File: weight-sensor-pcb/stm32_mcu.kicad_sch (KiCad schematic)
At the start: 1 part, among them U3 STM32G431KBTx

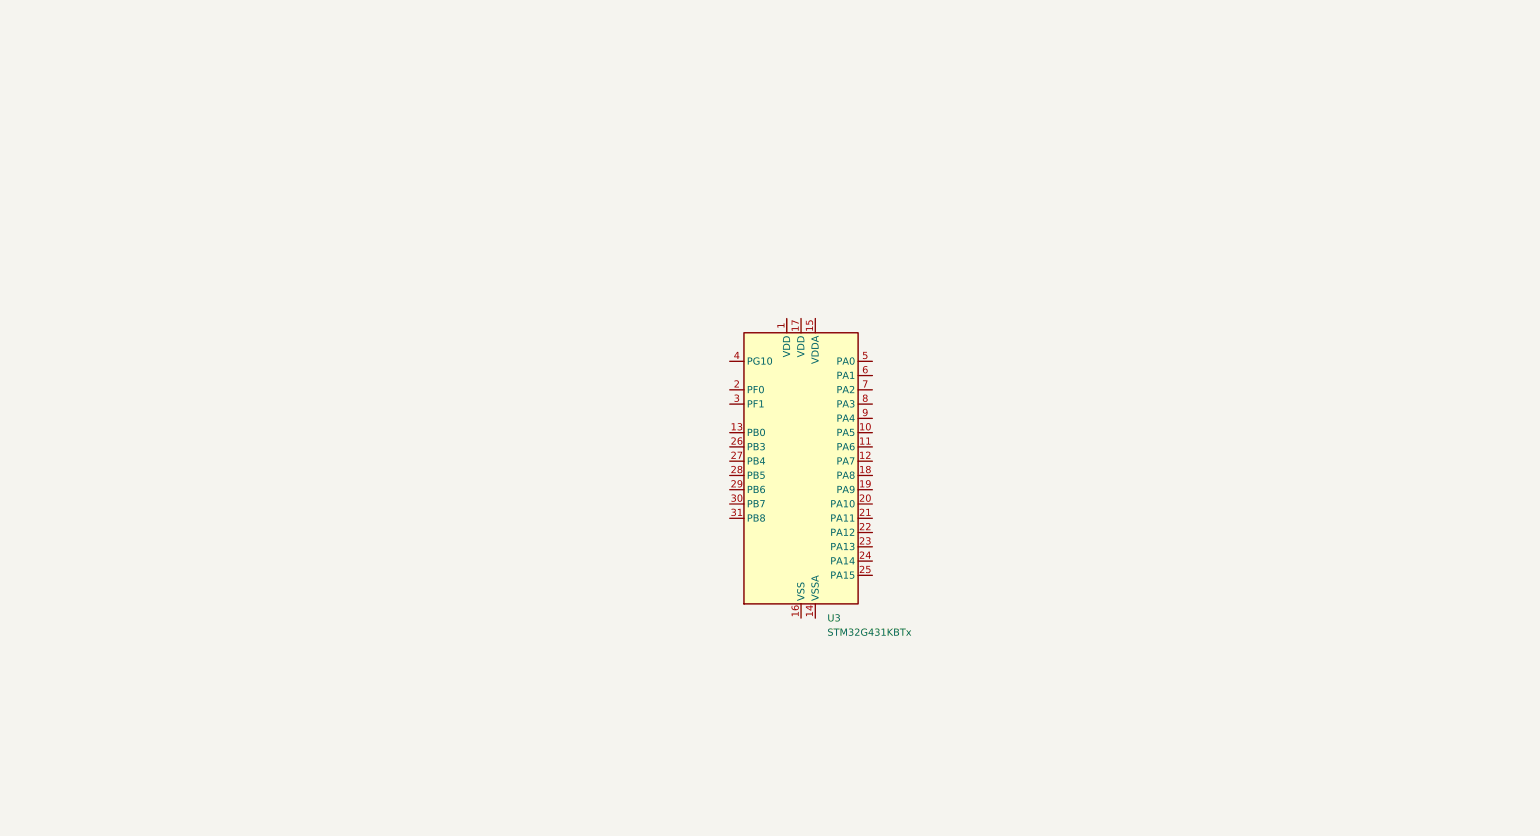
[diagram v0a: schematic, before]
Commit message: Swap MCU, add Library Loader integration
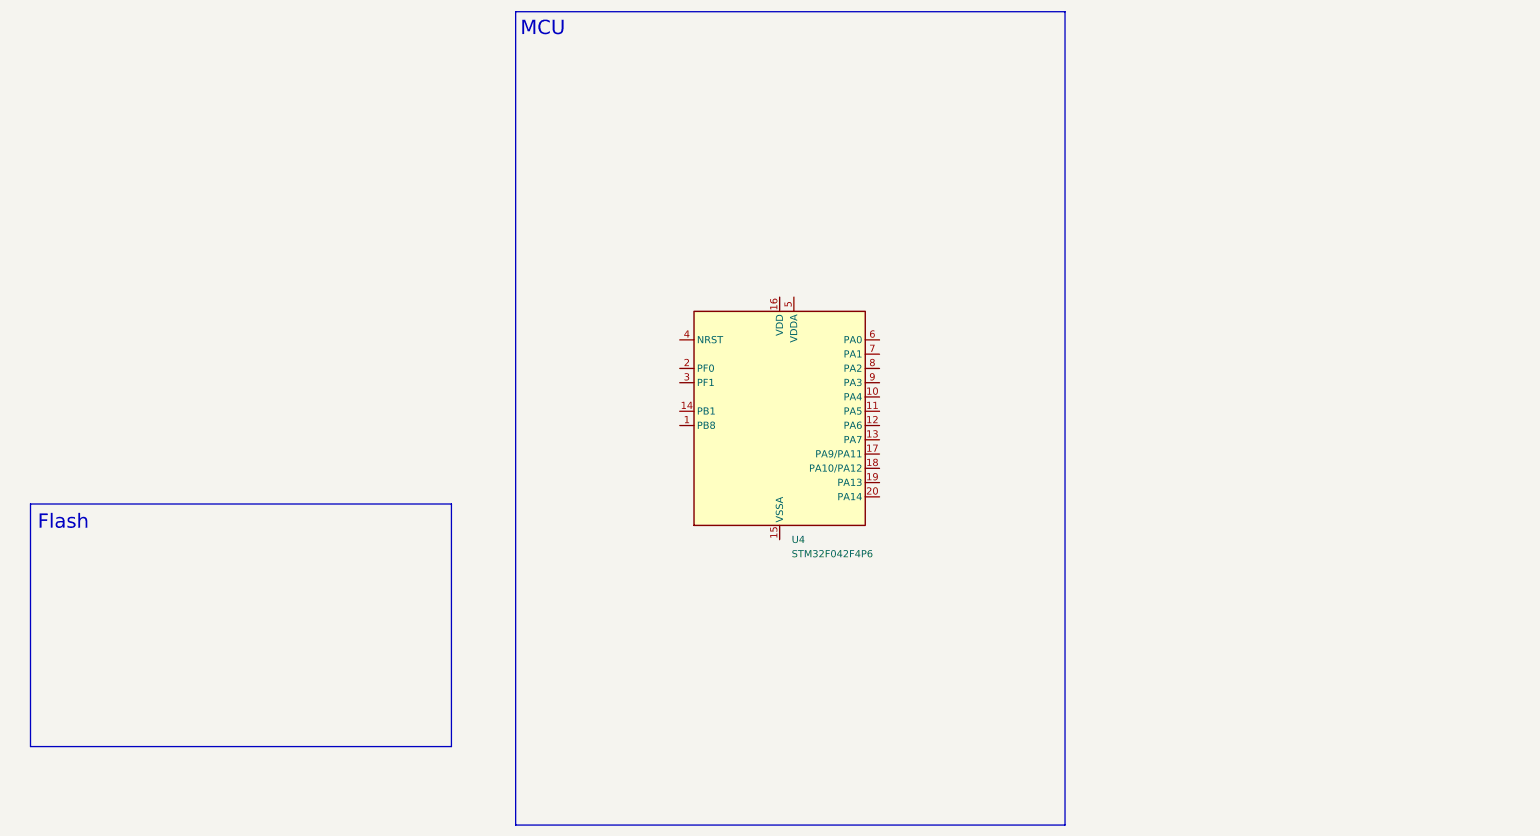
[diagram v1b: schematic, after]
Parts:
- removed U3: STM32G431KBTx, Package_QFP:LQFP-32_7x7mm_P0.8mm, symbol MCU_ST_STM32G4:STM32G431KBTx
- added U4: STM32F042F4P6, Package_SO:TSSOP-20_4.4x6.5mm_P0.65mm, symbol MCU_ST_STM32F0:STM32F042F4Px
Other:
- note added: "Flash"
- note added: "MCU"
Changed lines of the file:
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@@
 		(title "STM32 Microcontroller")
 	)
+	(rectangle
+		(start 15.24 101.6)
+		(end 90.17 144.78)
+		(stroke
+			(width 0)
+			(type default)
+		)
+		(fill
+			(type none)
+		)
+	)
+	(rectangle
+		(start 101.6 13.97)
+		(end 199.39 158.75)
+		(stroke
+			(width 0)
+			(type default)
+		)
+		(fill
+			(type none)
+		)
+	)
+	(text "Flash"
+		(exclude_from_sim no)
+		(at 21.082 104.902 0)
+		(effects
+			(font
+				(size 2.54 2.54)
+			)
+		)
+	)
+	(text "MCU"
+		(exclude_from_sim no)
+		(at 106.426 17.018 0)
+		(effects
+			(font
+				(size 2.54 2.54)
+			)
+		)
+	)
 	(symbol
-		(lib_id "MCU_ST_STM32G4:STM32G431KBTx")
-		(at 152.4 96.52 0)
+		(lib_id "MCU_ST_STM32F0:STM32F042F4Px")
+		(at 148.59 87.63 0)
 		(unit 1)
 		(exclude_from_sim no)
@@
 		(dnp no)
 		(fields_autoplaced yes)
-		(property "Reference" "U3"
-			(at 157.0833 121.92 0)
+		(property "Reference" "U4"
+			(at 150.7333 107.95 0)
 			(effects
 				(font
@@
 			)
 		)
-		(property "Value" "STM32G431KBTx"
-			(at 157.0833 124.46 0)
+		(property "Value" "STM32F042F4P6"
+			(at 150.7333 110.49 0)
 			(effects
 				(font
@@
 			)
 		)
-		(property "Footprint" "Package_QFP:LQFP-32_7x7mm_P0.8mm"
-			(at 142.24 119.38 0)
+		(property "Footprint" "Package_SO:TSSOP-20_4.4x6.5mm_P0.65mm"
+			(at 133.35 105.41 0)
 			(effects
 				(font
@@
 			)
 		)
-		(property "Datasheet" "https://www.st.com/resource/en/datasheet/stm32g431kb.pdf"
-			(at 152.4 96.52 0)
+		(property "Datasheet" "https://www.st.com/resource/en/datasheet/stm32f042f4.pdf"
+			(at 148.59 87.63 0)
 			(effects
 				(font
@@
 			)
 		)
-		(property "Description" "STMicroelectronics Arm Cortex-M4 MCU, 128KB flash, 32KB RAM, 170 MHz, 1.71-3.6V, 26 GPIO, LQFP32"
-			(at 152.4 96.52 0)
+		(property "Description" "STMicroelectronics Arm Cortex-M0 MCU, 16KB flash, 6KB RAM, 48 MHz, 2.0-3.6V, 16 GPIO, TSSOP20"
+			(at 148.59 87.63 0)
 			(effects
 				(font
@@
 			)
 		)
+		(pin "8"
+		)
+		(pin "7"
+		)
+		(pin "6"
+		)
+		(pin "17"
+		)
+		(pin "3"
+		)
+		(pin "10"
+		)
+		(pin "12"
+		)
+		(pin "13"
+		)
+		(pin "4"
+		)
+		(pin "1"
+		)
+		(pin "11"
+		)
 		(pin "18"
 		)
-		(pin "21"
+		(pin "16"
+		)
+		(pin "2"
+		)
+		(pin "9"
+		)
+		(pin "5"
+		)
+		(pin "14"
+		)
+		(pin "15"
 		)
 		(pin "20"
@@
 		(pin "19"
 		)
-		(pin "22"
-		)
-		(pin "23"
-		)
-		(pin "24"
-		)
-		(pin "25"
-		)
-		(pin "4"
-		)
-		(pin "2"
-		)
-		(pin "3"
-		)
-		(pin "13"
-		)
-		(pin "26"
-		)
-		(pin "27"
-		)
-		(pin "28"
-		)
-		(pin "29"
-		)
-		(pin "30"
-		)
-		(pin "31"
-		)
-		(pin "1"
-		)
-		(pin "17"
-		)
-		(pin "16"
-		)
-		(pin "32"
-		)
-		(pin "15"
-		)
-		(pin "14"
-		)
-		(pin "5"
-		)
-		(pin "6"
-		)
-		(pin "7"
-		)
-		(pin "8"
-		)
-		(pin "9"
-		)
-		(pin "10"
-		)
-		(pin "11"
-		)
-		(pin "12"
-		)
 		(instances
 			(project ""
 				(path "/030ca1f5-68f0-4323-9a91-656d7965b13e/d023421c-1516-46ef-aa61-fab015035186"
-					(reference "U3")
+					(reference "U4")
 					(unit 1)
 				)

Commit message: Add Serial Connection and CAN Transceiver
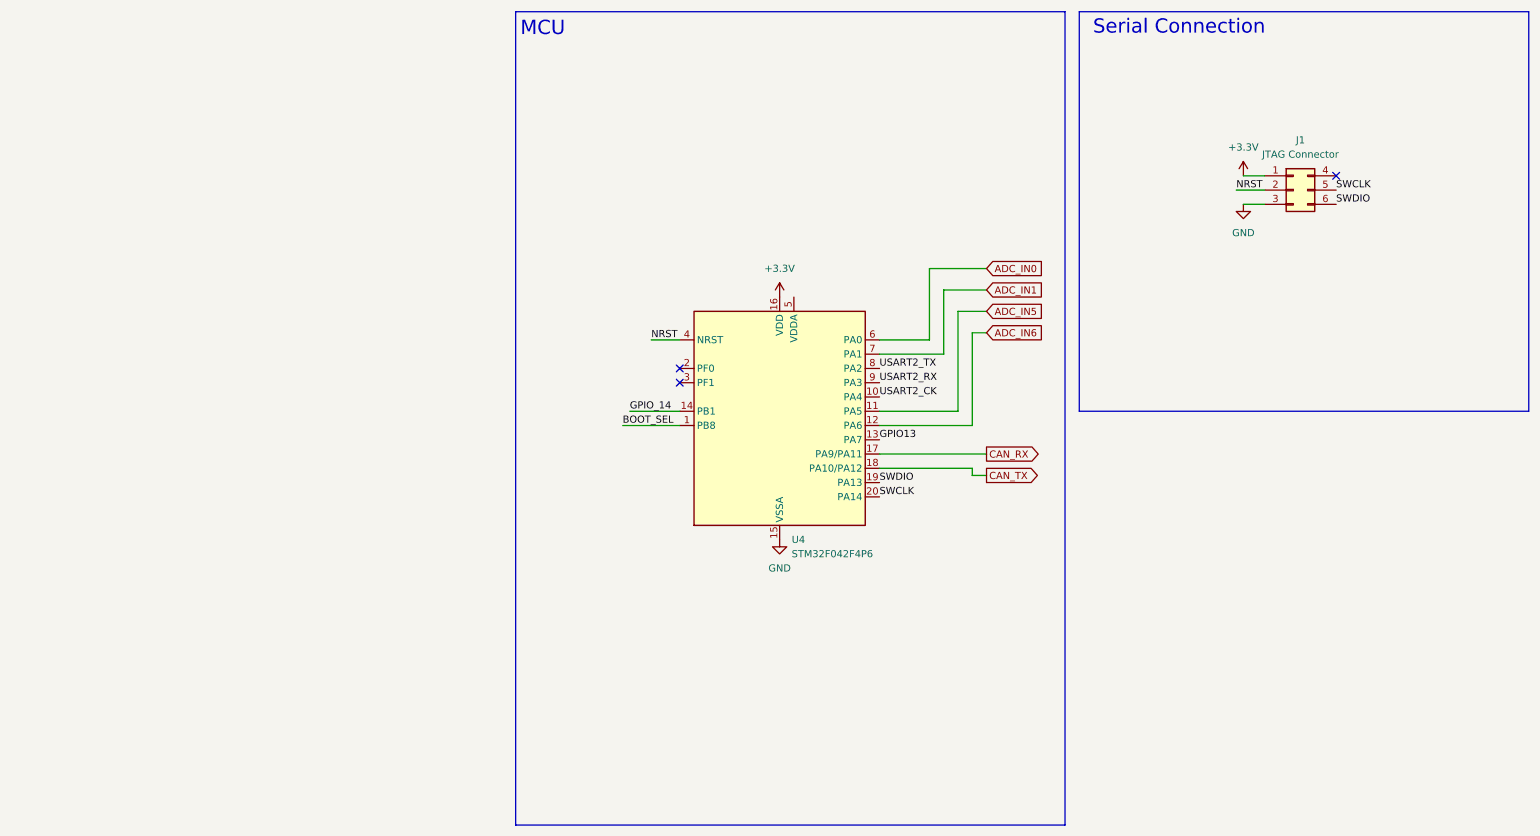
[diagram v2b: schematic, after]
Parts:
- added J1: JTAG Connector, Capstone:TC2030-IDC-NL, symbol Connector_Generic:Conn_02x03_Top_Bottom
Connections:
- net BOOT_SEL: now reaches U4.1 (PB8)
- net USART2_CK: now reaches U4.10 (PA4)
- net ADC_IN5: now reaches U4.11 (PA5)
- net ADC_IN6: now reaches U4.12 (PA6)
- net GPIO13: now reaches U4.13 (PA7)
- net GPIO_14: now reaches U4.14 (PB1)
- net GND: now reaches U4.15 (VSSA)
- net GND: now also J1.3 (Pin_3)
- net +3.3V: now reaches U4.16 (VDD)
- net +3.3V: now also J1.1 (Pin_1)
- net CAN_RX: now reaches U4.17 (PA9/PA11)
- net CAN_TX: now reaches U4.18 (PA10/PA12)
- net SWDIO: now reaches U4.19 (PA13)
- net SWDIO: now also J1.6 (Pin_6)
- net SWCLK: now reaches U4.20 (PA14)
- net SWCLK: now also J1.5 (Pin_5)
- net NRST: now reaches U4.4 (NRST)
- net NRST: now also J1.2 (Pin_2)
- net ADC_IN0: now reaches U4.6 (PA0)
- net ADC_IN1: now reaches U4.7 (PA1)
- net USART2_TX: now reaches U4.8 (PA2)
- net USART2_RX: now reaches U4.9 (PA3)
- no-connect marks 0 -> 3
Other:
- note added: "Serial Connection"
- note removed: "Flash"

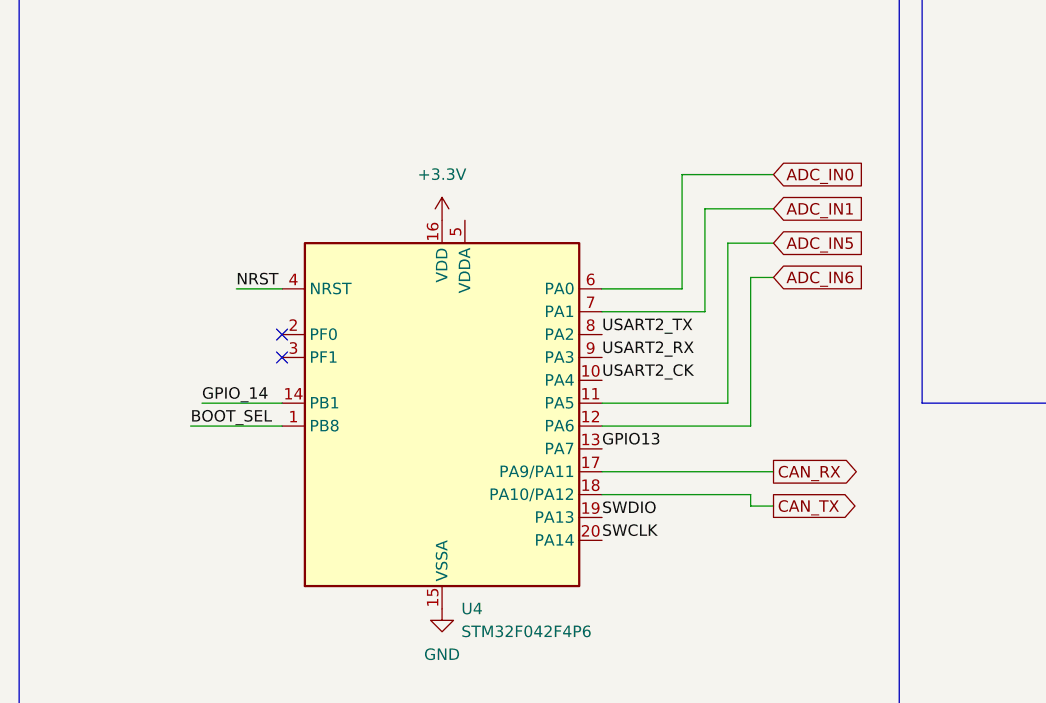
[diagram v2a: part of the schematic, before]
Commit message: Add hierarchial labels to MCU and CAN Interface sheets
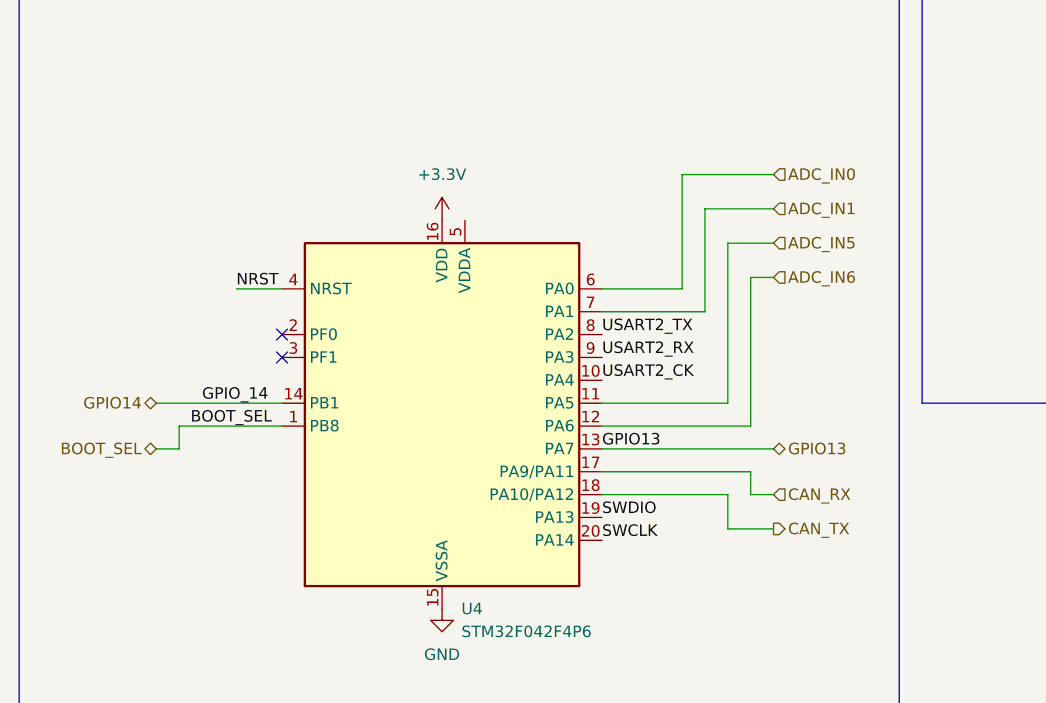
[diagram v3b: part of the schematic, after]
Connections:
- net GPIO_14 renamed GPIO14
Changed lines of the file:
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@@
 	(wire
 		(pts
-			(xy 120.65 87.63) (xy 130.81 87.63)
+			(xy 116.84 90.17) (xy 119.38 90.17)
 		)
 		(stroke
@@
 	(wire
 		(pts
+			(xy 182.88 92.71) (xy 166.37 92.71)
+		)
+		(stroke
+			(width 0)
+			(type default)
+		)
+	)
+	(wire
+		(pts
 			(xy 182.88 71.12) (xy 182.88 87.63)
 		)
@@
 	(wire
 		(pts
+			(xy 119.38 87.63) (xy 130.81 87.63)
+		)
+		(stroke
+			(width 0)
+			(type default)
+		)
+	)
+	(wire
+		(pts
 			(xy 175.26 59.69) (xy 175.26 72.39)
 		)
@@
 	(wire
 		(pts
-			(xy 121.92 85.09) (xy 130.81 85.09)
+			(xy 119.38 90.17) (xy 119.38 87.63)
+		)
+		(stroke
+			(width 0)
+			(type default)
+		)
+	)
+	(wire
+		(pts
+			(xy 185.42 90.17) (xy 166.37 90.17)
+		)
+		(stroke
+			(width 0)
+			(type default)
+		)
+	)
+	(wire
+		(pts
+			(xy 116.84 85.09) (xy 130.81 85.09)
 		)
 		(stroke
@@
 	(wire
 		(pts
-			(xy 185.42 96.52) (xy 182.88 96.52)
-		)
-		(stroke
-			(width 0)
-			(type default)
-		)
-	)
-	(wire
-		(pts
-			(xy 185.42 92.71) (xy 166.37 92.71)
+			(xy 185.42 99.06) (xy 180.34 99.06)
+		)
+		(stroke
+			(width 0)
+			(type default)
+		)
+	)
+	(wire
+		(pts
+			(xy 185.42 95.25) (xy 182.88 95.25)
 		)
 		(stroke
@@
 	(wire
 		(pts
-			(xy 182.88 95.25) (xy 166.37 95.25)
+			(xy 182.88 95.25) (xy 182.88 92.71)
+		)
+		(stroke
+			(width 0)
+			(type default)
+		)
+	)
+	(wire
+		(pts
+			(xy 180.34 95.25) (xy 166.37 95.25)
 		)
 		(stroke
@@
 	(wire
 		(pts
-			(xy 182.88 96.52) (xy 182.88 95.25)
+			(xy 180.34 99.06) (xy 180.34 95.25)
 		)
 		(stroke
@@
 		)
 	)
-	(global_label "CAN_TX"
+	(hierarchical_label "CAN_TX"
 		(shape output)
-		(at 185.42 96.52 0)
-		(fields_autoplaced yes)
-		(effects
-			(font
-				(size 1.27 1.27)
-			)
-			(justify left)
-		)
-		(property "Intersheetrefs" "${INTERSHEET_REFS}"
-			(at 195.239 96.52 0)
-			(effects
-				(font
-					(size 1.27 1.27)
-				)
-				(justify left)
-				(hide yes)
-			)
-		)
-	)
-	(global_label "ADC_IN5"
+		(at 185.42 99.06 0)
+		(effects
+			(font
+				(size 1.27 1.27)
+			)
+			(justify left)
+		)
+	)
+	(hierarchical_label "ADC_IN6"
+		(shape input)
+		(at 185.42 71.12 0)
+		(effects
+			(font
+				(size 1.27 1.27)
+			)
+			(justify left)
+		)
+	)
+	(hierarchical_label "GPIO13"
+		(shape bidirectional)
+		(at 185.42 90.17 0)
+		(effects
+			(font
+				(size 1.27 1.27)
+			)
+			(justify left)
+		)
+	)
+	(hierarchical_label "GPIO14"
+		(shape bidirectional)
+		(at 116.84 85.09 180)
+		(effects
+			(font
+				(size 1.27 1.27)
+			)
+			(justify right)
+		)
+	)
+	(hierarchical_label "ADC_IN5"
 		(shape input)
 		(at 185.42 67.31 0)
-		(fields_autoplaced yes)
-		(effects
-			(font
-				(size 1.27 1.27)
-			)
-			(justify left)
-		)
-		(property "Intersheetrefs" "${INTERSHEET_REFS}"
-			(at 196.1462 67.31 0)
-			(effects
-				(font
-					(size 1.27 1.27)
-				)
-				(justify left)
-				(hide yes)
-			)
-		)
-	)
-	(global_label "CAN_RX"
-		(shape output)
-		(at 185.42 92.71 0)
-		(fields_autoplaced yes)
-		(effects
-			(font
-				(size 1.27 1.27)
-			)
-			(justify left)
-		)
-		(property "Intersheetrefs" "${INTERSHEET_REFS}"
-			(at 195.5414 92.71 0)
-			(effects
-				(font
-					(size 1.27 1.27)
-				)
-				(justify left)
-				(hide yes)
-			)
-		)
-	)
-	(global_label "ADC_IN0"
+		(effects
+			(font
+				(size 1.27 1.27)
+			)
+			(justify left)
+		)
+	)
+	(hierarchical_label "CAN_RX"
+		(shape input)
+		(at 185.42 95.25 0)
+		(effects
+			(font
+				(size 1.27 1.27)
+			)
+			(justify left)
+		)
+	)
+	(hierarchical_label "ADC_IN0"
 		(shape input)
 		(at 185.42 59.69 0)
-		(fields_autoplaced yes)
-		(effects
-			(font
-				(size 1.27 1.27)
-			)
-			(justify left)
-		)
-		(property "Intersheetrefs" "${INTERSHEET_REFS}"
-			(at 196.1462 59.69 0)
-			(effects
-				(font
-					(size 1.27 1.27)
-				)
-				(justify left)
-				(hide yes)
-			)
-		)
-	)
-	(global_label "ADC_IN1"
+		(effects
+			(font
+				(size 1.27 1.27)
+			)
+			(justify left)
+		)
+	)
+	(hierarchical_label "BOOT_SEL"
+		(shape bidirectional)
+		(at 116.84 90.17 180)
+		(effects
+			(font
+				(size 1.27 1.27)
+			)
+			(justify right)
+		)
+	)
+	(hierarchical_label "ADC_IN1"
 		(shape input)
 		(at 185.42 63.5 0)
-		(fields_autoplaced yes)
-		(effects
-			(font
-				(size 1.27 1.27)
-			)
-			(justify left)
-		)
-		(property "Intersheetrefs" "${INTERSHEET_REFS}"
-			(at 196.1462 63.5 0)
-			(effects
-				(font
-					(size 1.27 1.27)
-				)
-				(justify left)
-				(hide yes)
-			)
-		)
-	)
-	(global_label "ADC_IN6"
-		(shape input)
-		(at 185.42 71.12 0)
-		(fields_autoplaced yes)
-		(effects
-			(font
-				(size 1.27 1.27)
-			)
-			(justify left)
-		)
-		(property "Intersheetrefs" "${INTERSHEET_REFS}"
-			(at 196.1462 71.12 0)
-			(effects
-				(font
-					(size 1.27 1.27)
-				)
-				(justify left)
-				(hide yes)
-			)
-		)
-	)
+		(effects
+			(font
+				(size 1.27 1.27)
+			)
+			(justify left)
+		)
+	)
